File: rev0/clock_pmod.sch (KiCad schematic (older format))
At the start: 5 parts, among them IC1 ECP5-BGA256, Y1 Osc60MHz

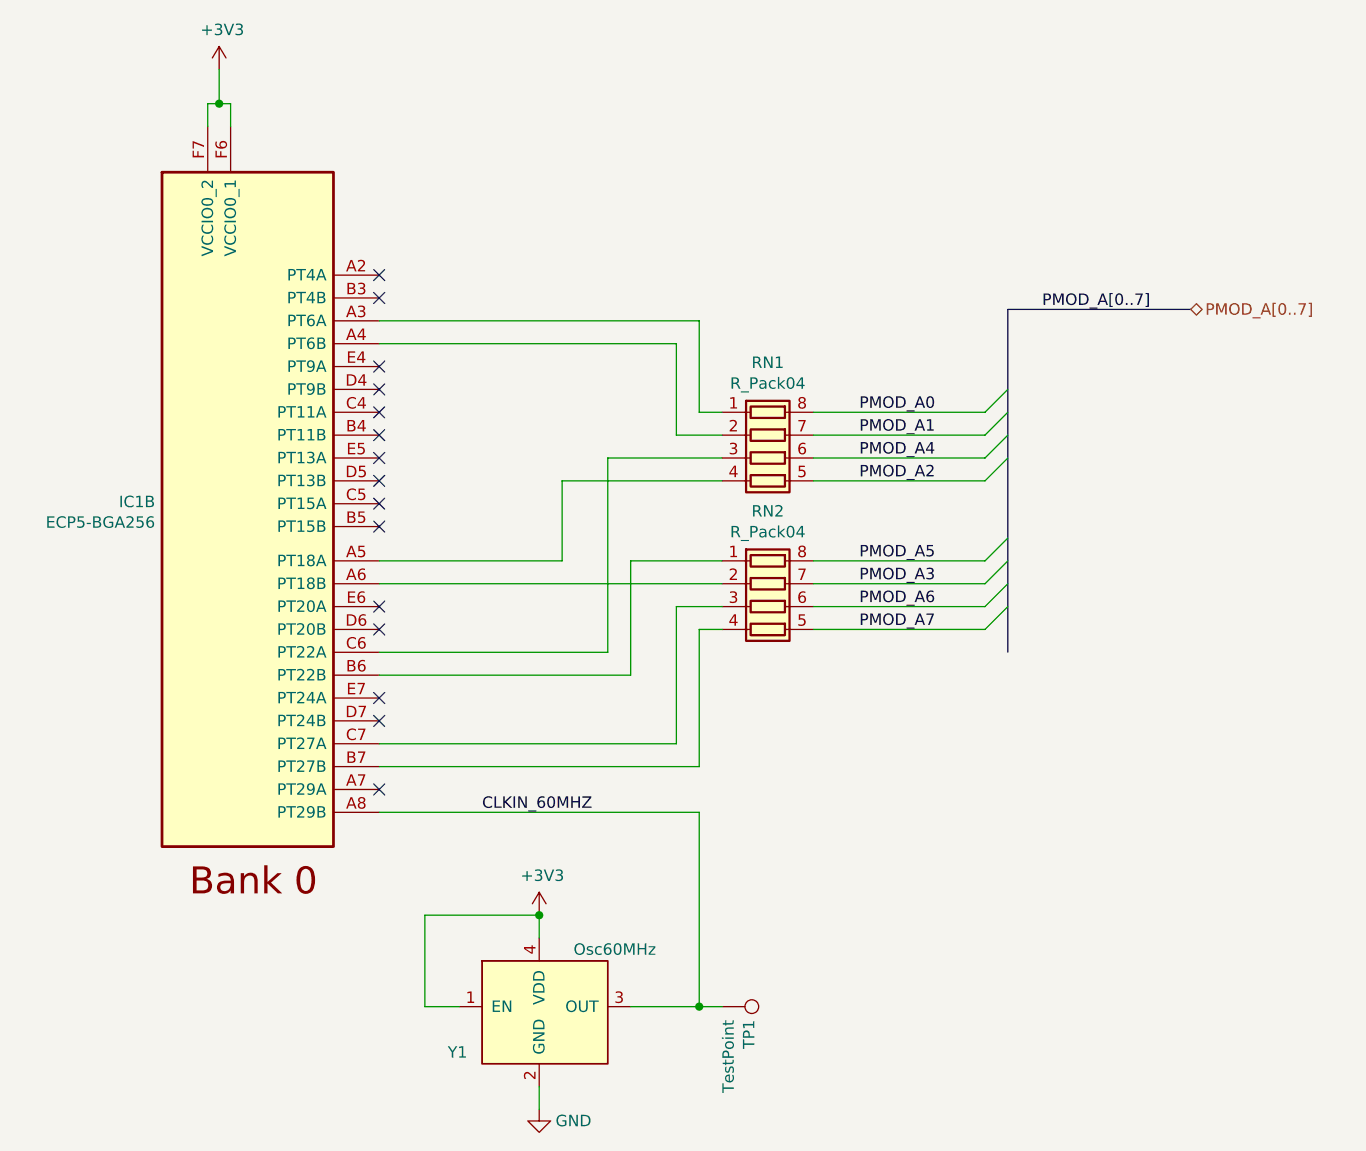
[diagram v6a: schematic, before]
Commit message: hardware: add more test points
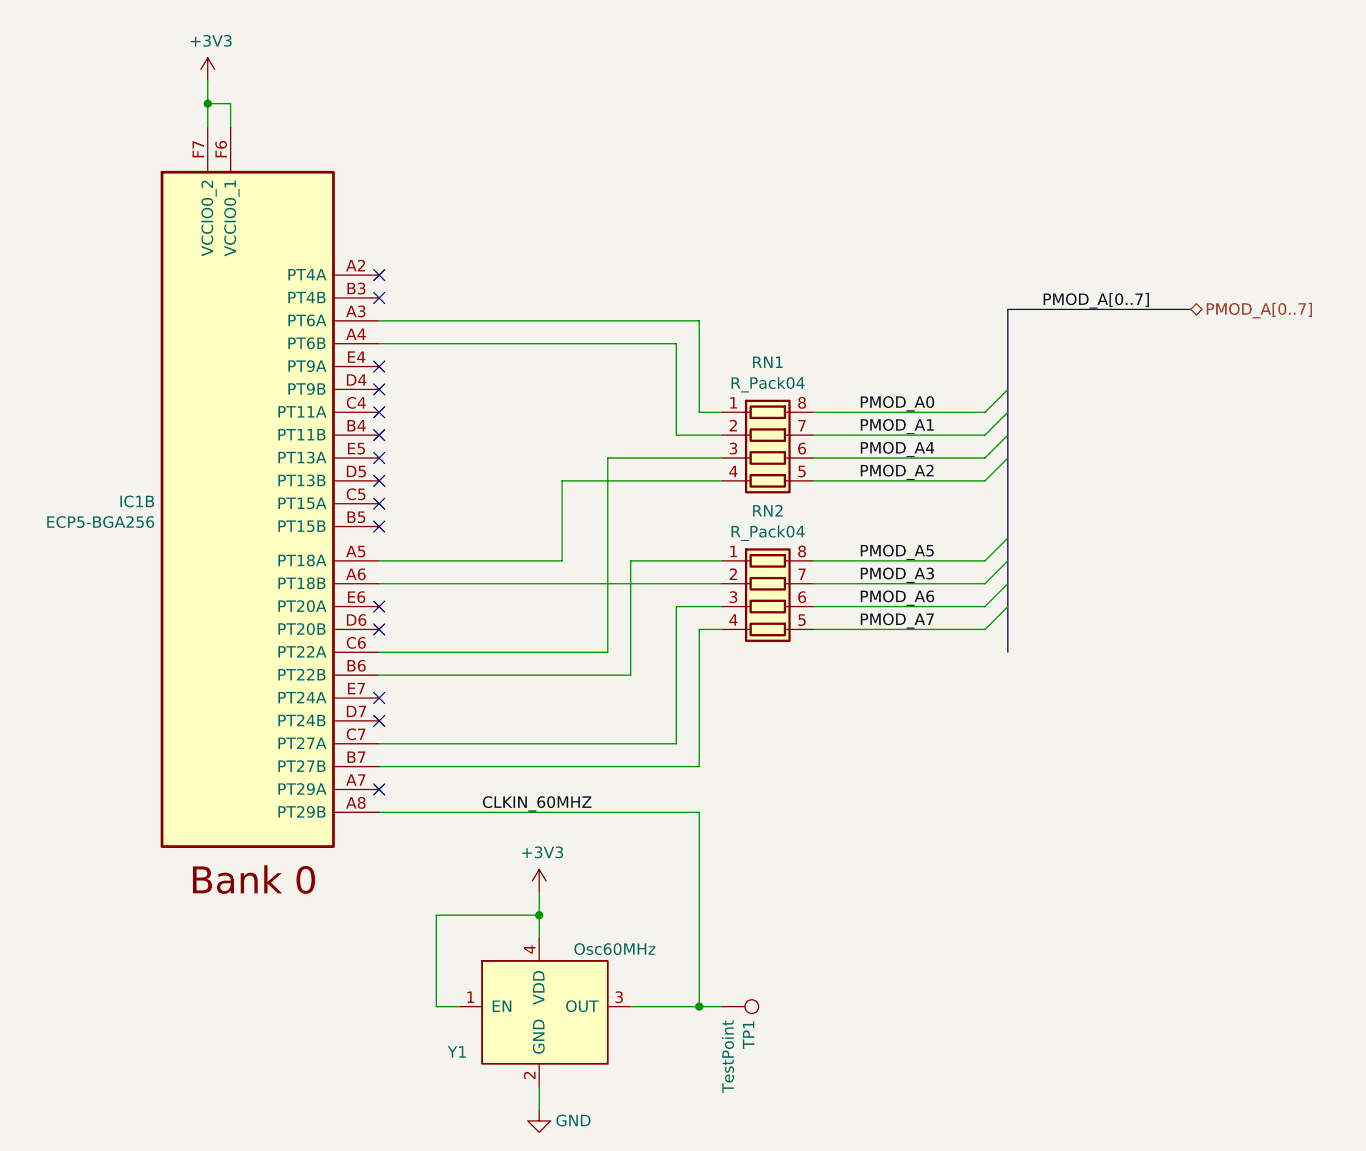
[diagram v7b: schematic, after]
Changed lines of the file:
@@
 $Descr A4 11693 8268
 encoding utf-8
-Sheet 9 9
+Sheet 8 9
 Title "LUNA: Clock and PMOD"
-Date "2021-01-04"
+Date "2021-01-05"
 Rev "r0"
 Comp "Copyright 2019-2021 Great Scott Gadgets"
@@
 	2400 1750 2400 1650
 Wire Wire Line
-	2400 1650 2450 1650
-Wire Wire Line
 	2500 1650 2500 1750
 Wire Wire Line
-	2450 1650 2450 1500
-Connection ~ 2450 1650
-Wire Wire Line
-	2450 1650 2500 1650
+	2400 1650 2400 1550
 NoConn ~ 3150 2500
 NoConn ~ 3150 2800
@@
 L power:+3V3 #PWR0105
 U 1 1 5E3ECE52
-P 2450 1500
-F 0 "#PWR0105" H 2450 1350 50  0001 C CNN
-F 1 "+3V3" H 2464 1673 50  0000 C CNN
-F 2 "" H 2450 1500 50  0001 C CNN
-F 3 "" H 2450 1500 50  0001 C CNN
-	1    2450 1500
+P 2400 1550
+F 0 "#PWR0105" H 2400 1400 50  0001 C CNN
+F 1 "+3V3" H 2414 1723 50  0000 C CNN
+F 2 "" H 2400 1550 50  0001 C CNN
+F 3 "" H 2400 1550 50  0001 C CNN
+	1    2400 1550
 	1    0    0    -1
 $EndComp
@@
 $EndComp
 Wire Wire Line
-	3500 5600 3350 5600
-Wire Wire Line
-	3350 5600 3350 5200
+	3500 5600 3400 5600
+Wire Wire Line
+	3400 5600 3400 5200
 Wire Wire Line
 	3850 5200 3850 5300
@@
 L power:+3V3 #PWR?
 U 1 1 604A6AA4
-P 3850 5200
+P 3850 5100
 AR Path="/604A6AA4" Ref="#PWR?"  Part="1"
 AR Path="/5DF88884/604A6AA4" Ref="#PWR011"  Part="1"
-F 0 "#PWR011" H 3850 5050 50  0001 C CNN
-F 1 "+3V3" H 3864 5373 50  0000 C CNN
-F 2 "" H 3850 5200 50  0001 C CNN
-F 3 "" H 3850 5200 50  0001 C CNN
-	1    3850 5200
+F 0 "#PWR011" H 3850 4950 50  0001 C CNN
+F 1 "+3V3" H 3864 5273 50  0000 C CNN
+F 2 "" H 3850 5100 50  0001 C CNN
+F 3 "" H 3850 5100 50  0001 C CNN
+	1    3850 5100
 	1    0    0    -1
 $EndComp
@@
 	3850 6050 3850 5950
 Wire Wire Line
-	3350 5200 3850 5200
+	3400 5200 3850 5200
 Connection ~ 3850 5200
 $Comp
@@
 Entry Wire Line
 	5800 3950 5900 3850
+Wire Wire Line
+	3850 5100 3850 5200
+Connection ~ 2400 1650
+Wire Wire Line
+	2400 1650 2500 1650
 Wire Bus Line
 	5900 2550 5900 4050

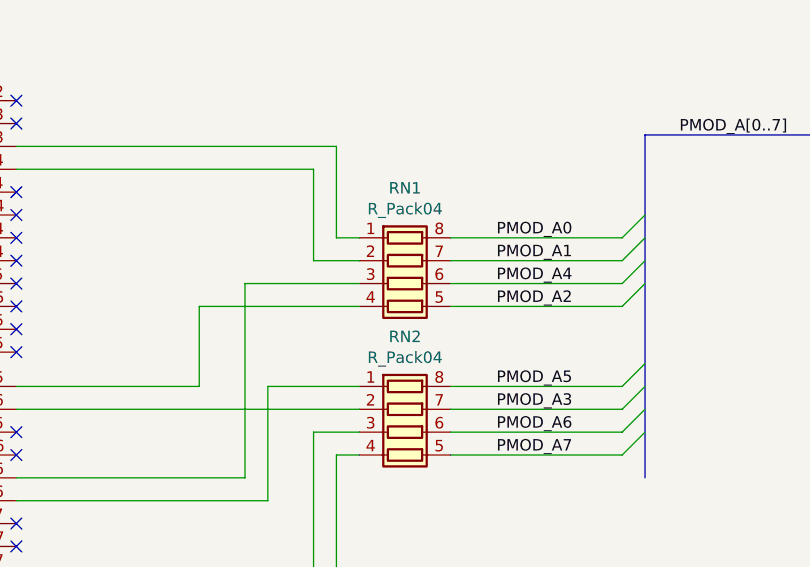
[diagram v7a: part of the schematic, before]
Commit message: hardware: clarify schematic
specify CC resistors as ±10% to hint that the spec requires it
add resistance value to resistor networks
give UART nets top-level names indicating JTAG functions
change AP22811 values to AP22811A
change PMOD to Pmod
nudge FPGA_TMS trace to make it more bodgeable
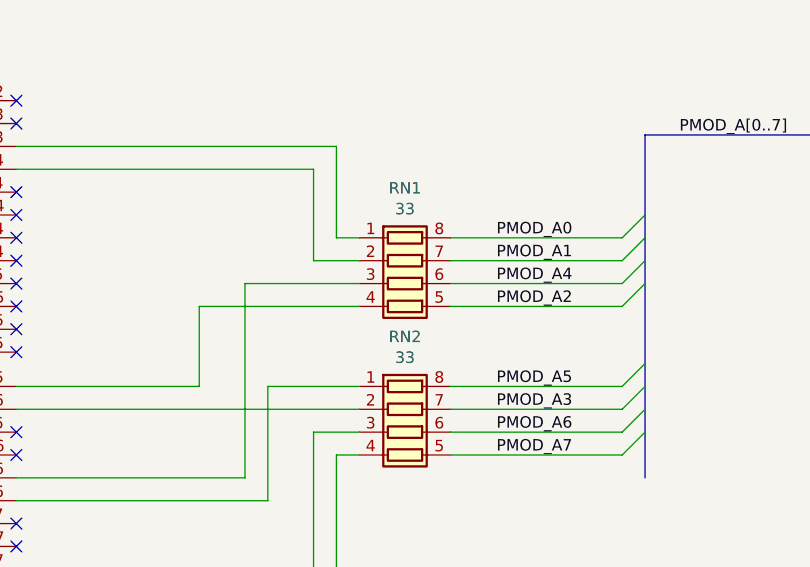
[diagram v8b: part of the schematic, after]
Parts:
- RN1, RN2: value R_Pack04 -> 33
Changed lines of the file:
@@
 Sheet 8 9
 Title "LUNA: Clock and PMOD"
-Date "2021-01-05"
+Date "2021-01-08"
 Rev "r0"
 Comp "Copyright 2019-2021 Great Scott Gadgets"
@@
 AR Path="/5DF88884/61658D8E" Ref="RN1"  Part="1"
 F 0 "RN1" V 4433 3200 50  0000 C CNN
-F 1 "R_Pack04" V 4524 3200 50  0000 C CNN
+F 1 "33" V 4524 3200 50  0000 C CNN
 F 2 "Resistor_SMD:R_Array_Convex_4x0402" V 5125 3200 50  0001 C CNN
 F 3 "~" H 4850 3200 50  0001 C CNN
@@
 AR Path="/5DF88884/61658D97" Ref="RN2"  Part="1"
 F 0 "RN2" V 4433 3850 50  0000 C CNN
-F 1 "R_Pack04" V 4524 3850 50  0000 C CNN
+F 1 "33" V 4524 3850 50  0000 C CNN
 F 2 "Resistor_SMD:R_Array_Convex_4x0402" V 5125 3850 50  0001 C CNN
 F 3 "~" H 4850 3850 50  0001 C CNN
